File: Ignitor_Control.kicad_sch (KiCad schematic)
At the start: 12 parts, among them J21 Ignitor Screw Terminal, K2 G5Q-1A DC24, Q8 BSS138, U9 INA199A2DCK

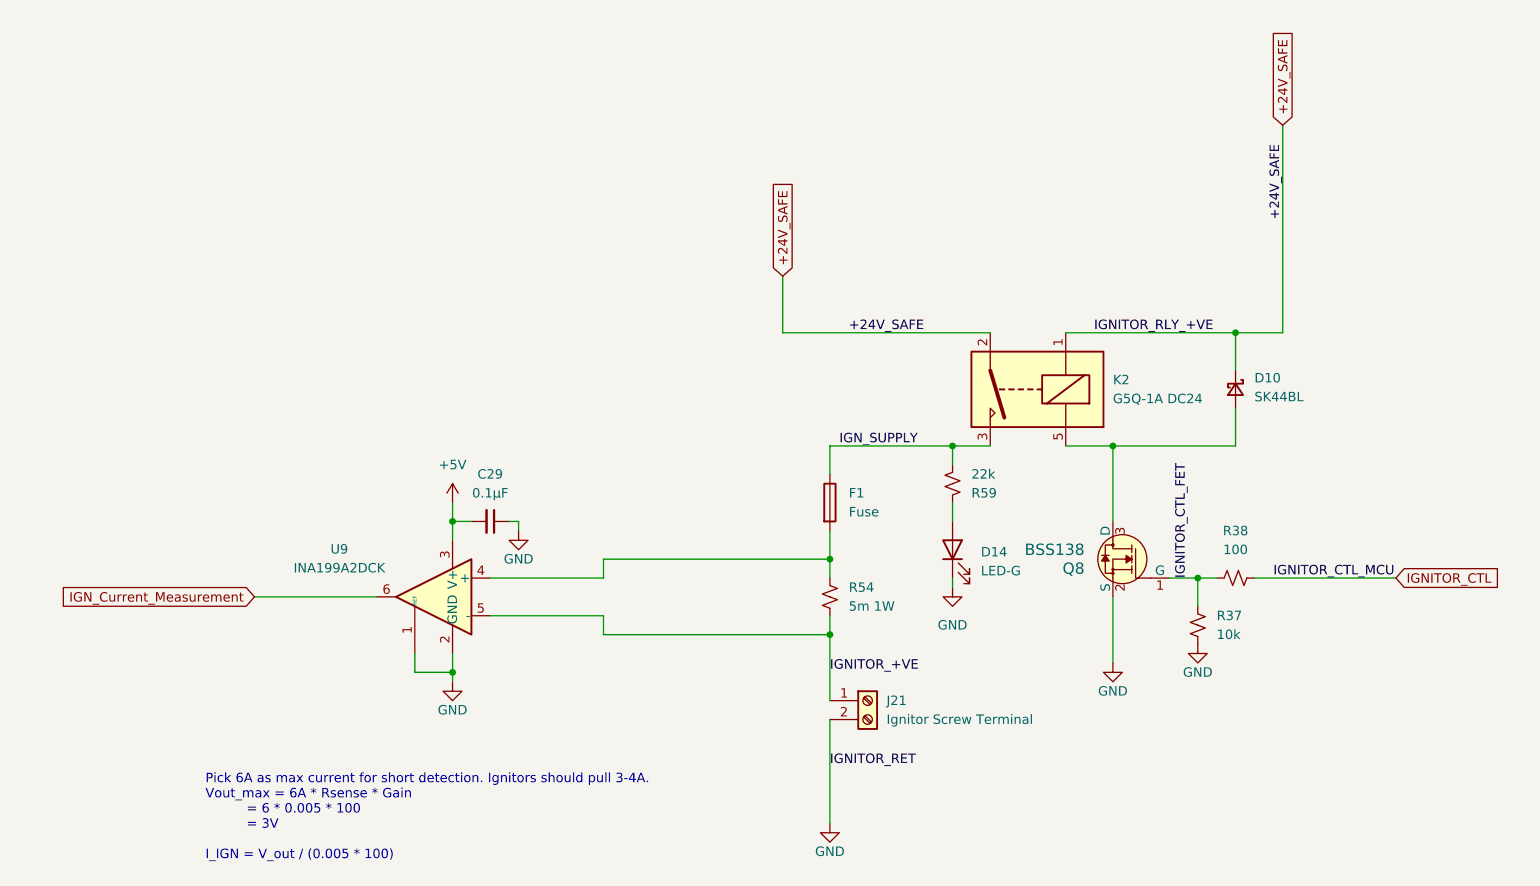
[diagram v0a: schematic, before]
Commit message: connected to GPIO pins
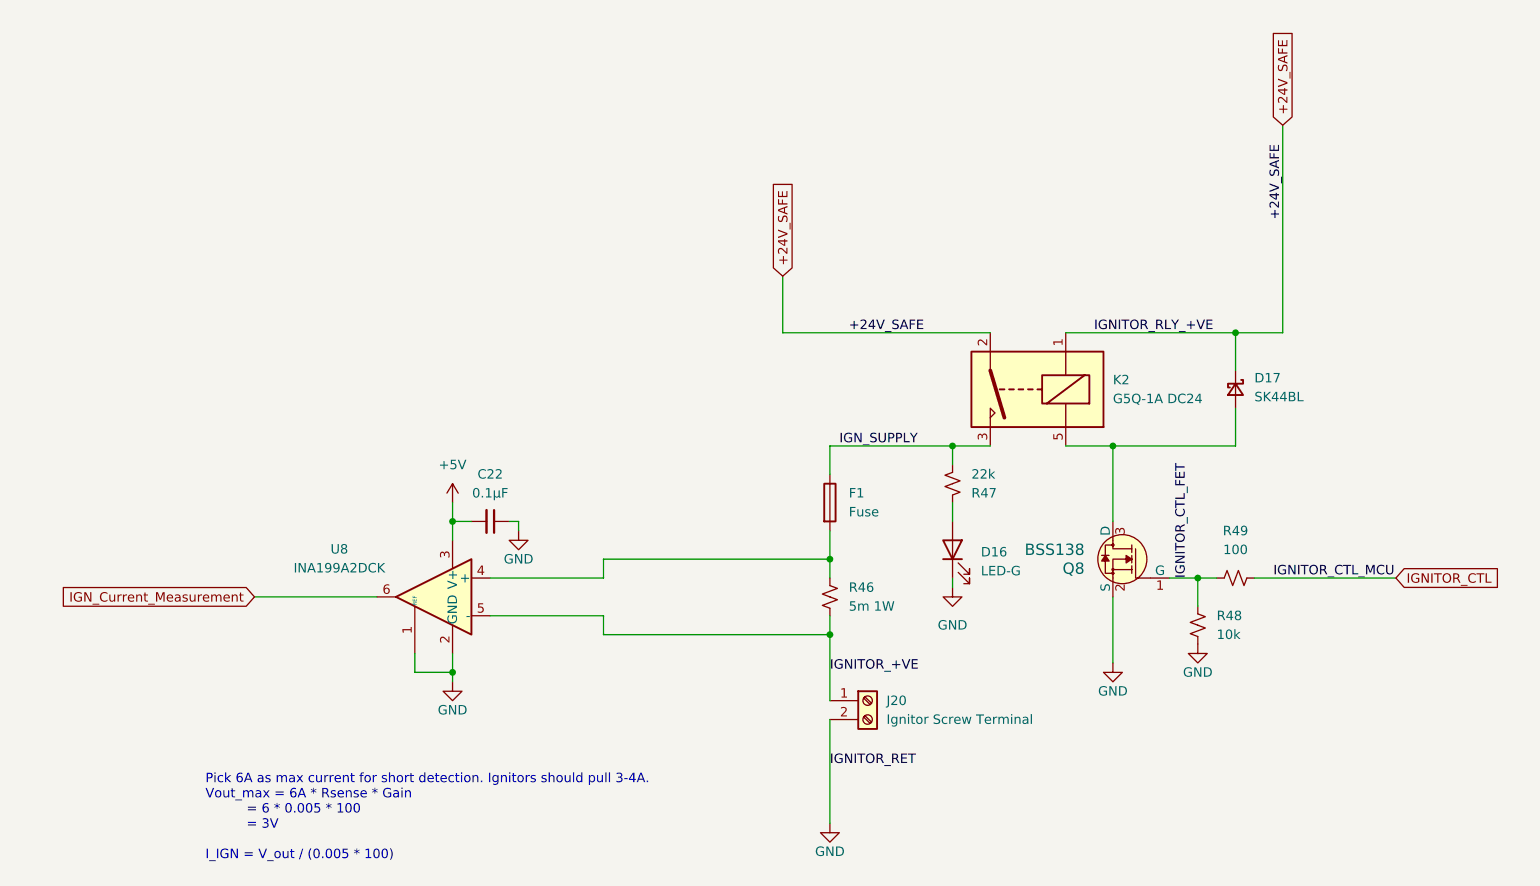
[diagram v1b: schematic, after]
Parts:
- renumbered C29 to C22, D14 to D16, D10 to D17, J21 to J20, R54 to R46, R59 to R47, R37 to R48, R38 to R49, U9 to U8
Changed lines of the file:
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@@
 		(dnp no)
 		(fields_autoplaced yes)
-		(property "Reference" "D14"
+		(property "Reference" "D16"
 			(at 182.88 103.1874 90)
 			(effects
@@
 			(project "panda"
 				(path "/226c5870-4123-4efa-a2b3-b42d02f59bb7/4e09186f-4067-4c22-bbd5-0048a728fd95"
-					(reference "D14")
+					(reference "D16")
 					(unit 1)
 				)
@@
 		(dnp no)
 		(fields_autoplaced yes)
-		(property "Reference" "#PWR0116"
+		(property "Reference" "#PWR0114"
 			(at 111.76 100.33 0)
 			(effects
@@
 			(project "panda"
 				(path "/226c5870-4123-4efa-a2b3-b42d02f59bb7/4e09186f-4067-4c22-bbd5-0048a728fd95"
-					(reference "#PWR0116")
+					(reference "#PWR0114")
 					(unit 1)
 				)
@@
 		(dnp no)
 		(fields_autoplaced yes)
-		(property "Reference" "R54"
+		(property "Reference" "R46"
 			(at 165.1 107.9499 0)
 			(effects
@@
 			(project ""
 				(path "/226c5870-4123-4efa-a2b3-b42d02f59bb7/4e09186f-4067-4c22-bbd5-0048a728fd95"
-					(reference "R54")
+					(reference "R46")
 					(unit 1)
 				)
@@
 		(dnp no)
 		(fields_autoplaced yes)
-		(property "Reference" "#PWR0123"
+		(property "Reference" "#PWR0118"
 			(at 179.07 114.3 0)
 			(effects
@@
 			(project "panda"
 				(path "/226c5870-4123-4efa-a2b3-b42d02f59bb7/4e09186f-4067-4c22-bbd5-0048a728fd95"
-					(reference "#PWR0123")
+					(reference "#PWR0118")
 					(unit 1)
 				)
@@
 		(on_board yes)
 		(dnp no)
-		(property "Reference" "#PWR098"
+		(property "Reference" "#PWR0117"
 			(at 162.56 146.05 0)
 			(effects
@@
 			(project "nexus"
 				(path "/226c5870-4123-4efa-a2b3-b42d02f59bb7/4e09186f-4067-4c22-bbd5-0048a728fd95"
-					(reference "#PWR098")
+					(reference "#PWR0117")
 					(unit 1)
 				)
@@
 		(on_board yes)
 		(dnp no)
-		(property "Reference" "U9"
+		(property "Reference" "U8"
 			(at 96.52 102.7998 0)
 			(effects
@@
 			(project ""
 				(path "/226c5870-4123-4efa-a2b3-b42d02f59bb7/4e09186f-4067-4c22-bbd5-0048a728fd95"
-					(reference "U9")
+					(reference "U8")
 					(unit 1)
 				)
@@
 		(on_board yes)
 		(dnp no)
-		(property "Reference" "#PWR099"
+		(property "Reference" "#PWR0119"
 			(at 200.66 124.46 0)
 			(effects
@@
 			(project "nexus"
 				(path "/226c5870-4123-4efa-a2b3-b42d02f59bb7/4e09186f-4067-4c22-bbd5-0048a728fd95"
-					(reference "#PWR099")
+					(reference "#PWR0119")
 					(unit 1)
 				)
@@
 		(dnp no)
 		(fields_autoplaced yes)
-		(property "Reference" "J21"
+		(property "Reference" "J20"
 			(at 170.18 123.1899 0)
 			(effects
@@
 			(project ""
 				(path "/226c5870-4123-4efa-a2b3-b42d02f59bb7/4e09186f-4067-4c22-bbd5-0048a728fd95"
-					(reference "J21")
+					(reference "J20")
 					(unit 1)
 				)
@@
 		(dnp no)
 		(fields_autoplaced yes)
-		(property "Reference" "R37"
+		(property "Reference" "R48"
 			(at 214.63 111.7599 0)
 			(effects
@@
 			(project "panda"
 				(path "/226c5870-4123-4efa-a2b3-b42d02f59bb7/4e09186f-4067-4c22-bbd5-0048a728fd95"
-					(reference "R37")
+					(reference "R48")
 					(unit 1)
 				)
@@
 		(dnp no)
 		(fields_autoplaced yes)
-		(property "Reference" "D10"
+		(property "Reference" "D17"
 			(at 219.71 79.7559 90)
 			(effects
@@
 			(project "nexus"
 				(path "/226c5870-4123-4efa-a2b3-b42d02f59bb7/4e09186f-4067-4c22-bbd5-0048a728fd95"
-					(reference "D10")
+					(reference "D17")
 					(unit 1)
 				)
@@
 		(on_board yes)
 		(dnp no)
-		(property "Reference" "#PWR0117"
+		(property "Reference" "#PWR0116"
 			(at 120.65 106.68 0)
 			(effects
@@
 			(project "panda"
 				(path "/226c5870-4123-4efa-a2b3-b42d02f59bb7/4e09186f-4067-4c22-bbd5-0048a728fd95"
-					(reference "#PWR0117")
+					(reference "#PWR0116")
 					(unit 1)
 				)
@@
 		(on_board yes)
 		(dnp no)
-		(property "Reference" "#PWR0100"
+		(property "Reference" "#PWR0120"
 			(at 212.09 121.92 0)
 			(effects
@@
 			(project "panda"
 				(path "/226c5870-4123-4efa-a2b3-b42d02f59bb7/4e09186f-4067-4c22-bbd5-0048a728fd95"
-					(reference "#PWR0100")
+					(reference "#PWR0120")
 					(unit 1)
 				)
@@
 		(dnp no)
 		(fields_autoplaced yes)
-		(property "Reference" "C29"
+		(property "Reference" "C22"
 			(at 116.8337 92.71 90)
 			(effects
@@
 			(project "panda"
 				(path "/226c5870-4123-4efa-a2b3-b42d02f59bb7/4e09186f-4067-4c22-bbd5-0048a728fd95"
-					(reference "C29")
+					(reference "C22")
 					(unit 1)
 				)
@@
 		(dnp no)
 		(fields_autoplaced yes)
-		(property "Reference" "R59"
+		(property "Reference" "R47"
 			(at 181.61 95.2501 0)
 			(effects
@@
 			(project "panda"
 				(path "/226c5870-4123-4efa-a2b3-b42d02f59bb7/4e09186f-4067-4c22-bbd5-0048a728fd95"
-					(reference "R59")
+					(reference "R47")
 					(unit 1)
 				)
@@
 		(dnp no)
 		(fields_autoplaced yes)
-		(property "Reference" "R38"
+		(property "Reference" "R49"
 			(at 217.17 100.33 90)
 			(effects
@@
 			(project "panda"
 				(path "/226c5870-4123-4efa-a2b3-b42d02f59bb7/4e09186f-4067-4c22-bbd5-0048a728fd95"
-					(reference "R38")
-					(unit 1)
-				)
+					(reference "R49")
+					(unit 1)
+				)

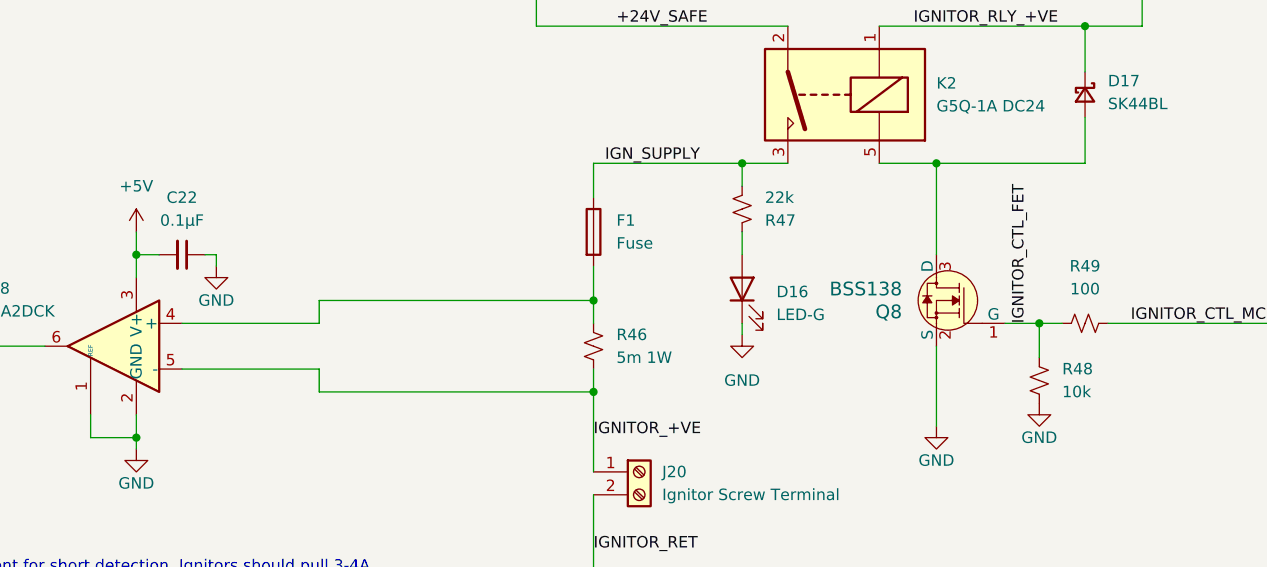
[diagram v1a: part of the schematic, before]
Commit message: added 24V lockout key LED indicator
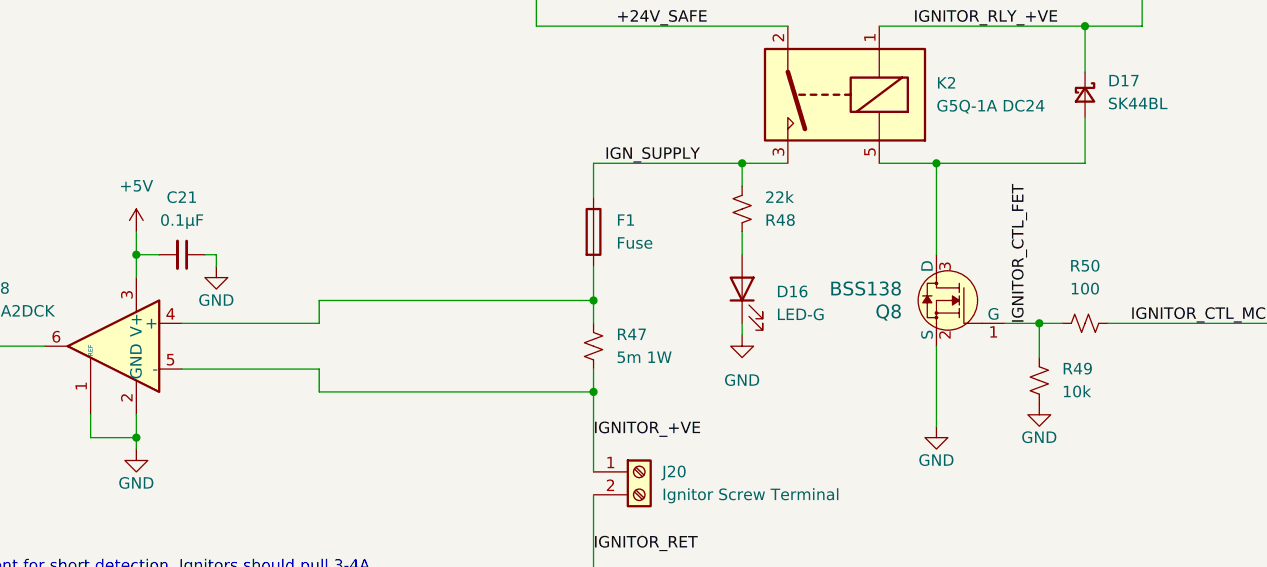
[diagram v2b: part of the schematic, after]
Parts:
- renumbered C22 to C21, R46 to R47, R47 to R48, R48 to R49, R49 to R50
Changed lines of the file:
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@@
 		(dnp no)
 		(fields_autoplaced yes)
-		(property "Reference" "R46"
+		(property "Reference" "R47"
 			(at 165.1 107.9499 0)
 			(effects
@@
 			(project ""
 				(path "/226c5870-4123-4efa-a2b3-b42d02f59bb7/4e09186f-4067-4c22-bbd5-0048a728fd95"
-					(reference "R46")
+					(reference "R47")
 					(unit 1)
 				)
@@
 		(dnp no)
 		(fields_autoplaced yes)
-		(property "Reference" "R48"
+		(property "Reference" "R49"
 			(at 214.63 111.7599 0)
 			(effects
@@
 			(project "panda"
 				(path "/226c5870-4123-4efa-a2b3-b42d02f59bb7/4e09186f-4067-4c22-bbd5-0048a728fd95"
-					(reference "R48")
+					(reference "R49")
 					(unit 1)
 				)
@@
 		(dnp no)
 		(fields_autoplaced yes)
-		(property "Reference" "C22"
+		(property "Reference" "C21"
 			(at 116.8337 92.71 90)
 			(effects
@@
 			(project "panda"
 				(path "/226c5870-4123-4efa-a2b3-b42d02f59bb7/4e09186f-4067-4c22-bbd5-0048a728fd95"
-					(reference "C22")
+					(reference "C21")
 					(unit 1)
 				)
@@
 		(dnp no)
 		(fields_autoplaced yes)
-		(property "Reference" "R47"
+		(property "Reference" "R48"
 			(at 181.61 95.2501 0)
 			(effects
@@
 			(project "panda"
 				(path "/226c5870-4123-4efa-a2b3-b42d02f59bb7/4e09186f-4067-4c22-bbd5-0048a728fd95"
-					(reference "R47")
+					(reference "R48")
 					(unit 1)
 				)
@@
 		(dnp no)
 		(fields_autoplaced yes)
-		(property "Reference" "R49"
+		(property "Reference" "R50"
 			(at 217.17 100.33 90)
 			(effects
@@
 			(project "panda"
 				(path "/226c5870-4123-4efa-a2b3-b42d02f59bb7/4e09186f-4067-4c22-bbd5-0048a728fd95"
-					(reference "R49")
-					(unit 1)
-				)
+					(reference "R50")
+					(unit 1)
+				)

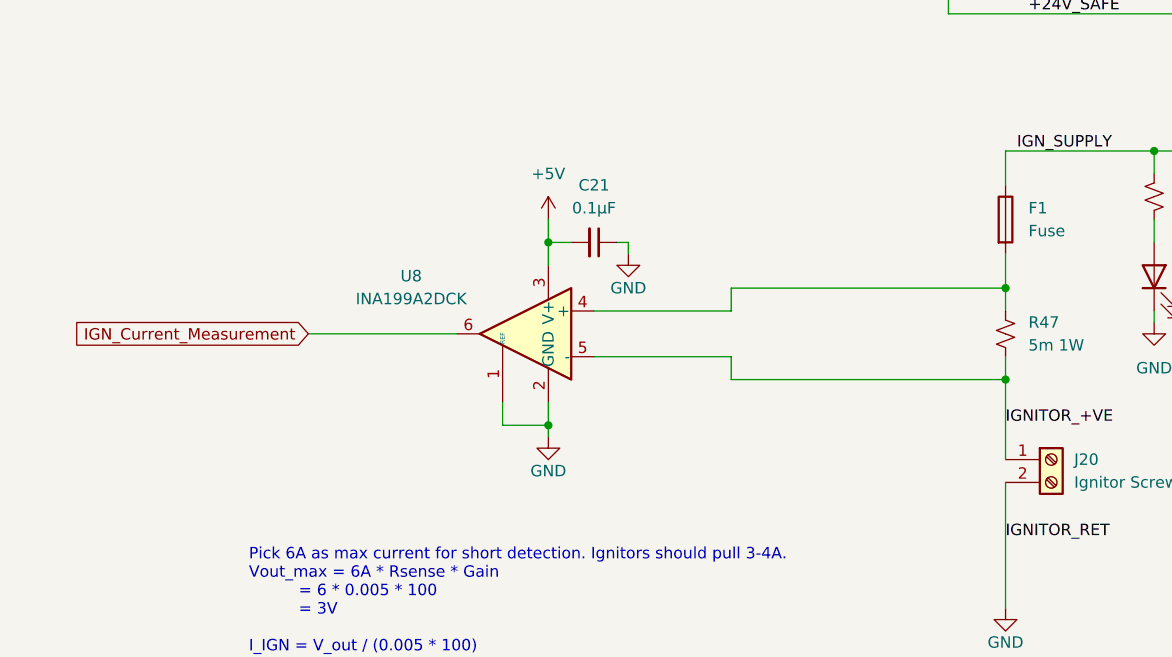
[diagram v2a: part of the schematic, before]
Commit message: added ignitor current sensor overvoltage protection
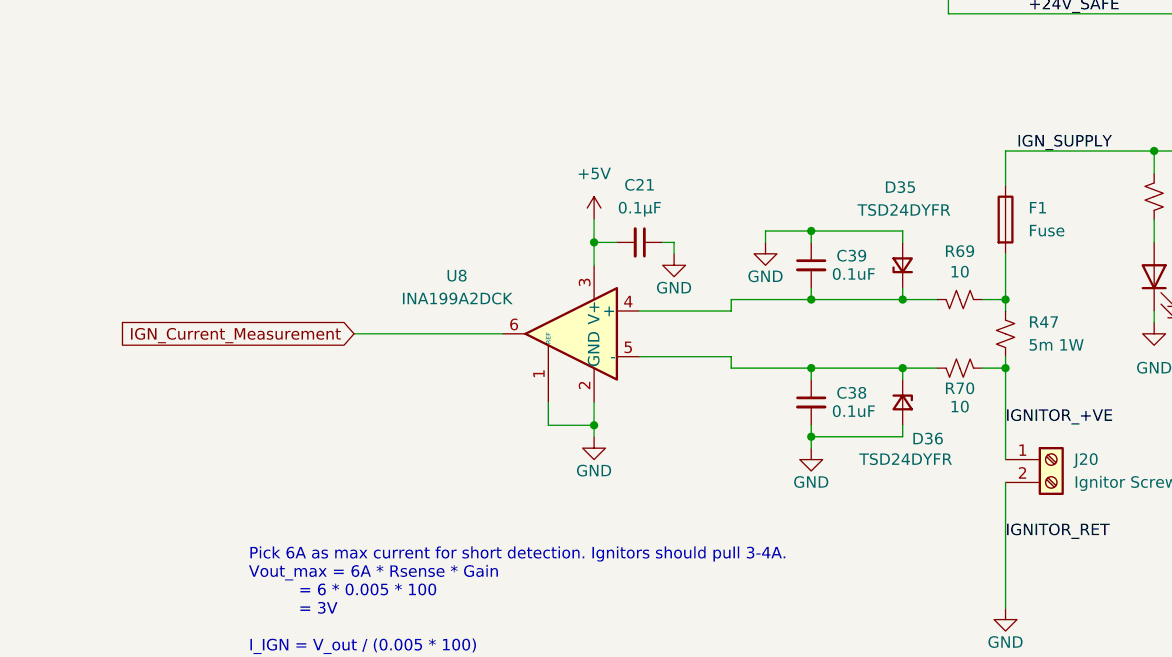
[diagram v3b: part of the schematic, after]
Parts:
- added C38, C39: 0.1uF, symbol Device:C_Small
- added D35, D36: TSD24DYFR, symbol Device:D_Zener_Small
- added R69, R70: 10, Resistor_SMD:R_0402_1005Metric, symbol Device:R_Small_US
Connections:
- net GND: now also C38.2, C39.1, D35.2 (A), D36.2 (A)
- net IGNITOR_+VE: now also R70.1; no longer U8.5 (-)
- net at F1.2, R47.1: now also R69.1; no longer U8.4 (+)
- new net: C38.1, D36.1 (K), R70.2, U8.5 (-)
- new net: C39.2, D35.1 (K), R69.2, U8.4 (+)
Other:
- moved on the sheet: C21, U8
